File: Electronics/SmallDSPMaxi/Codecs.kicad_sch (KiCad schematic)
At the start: 56 parts, among them J13 IDC, J14 IDC, J15 IDC, J16 IDC

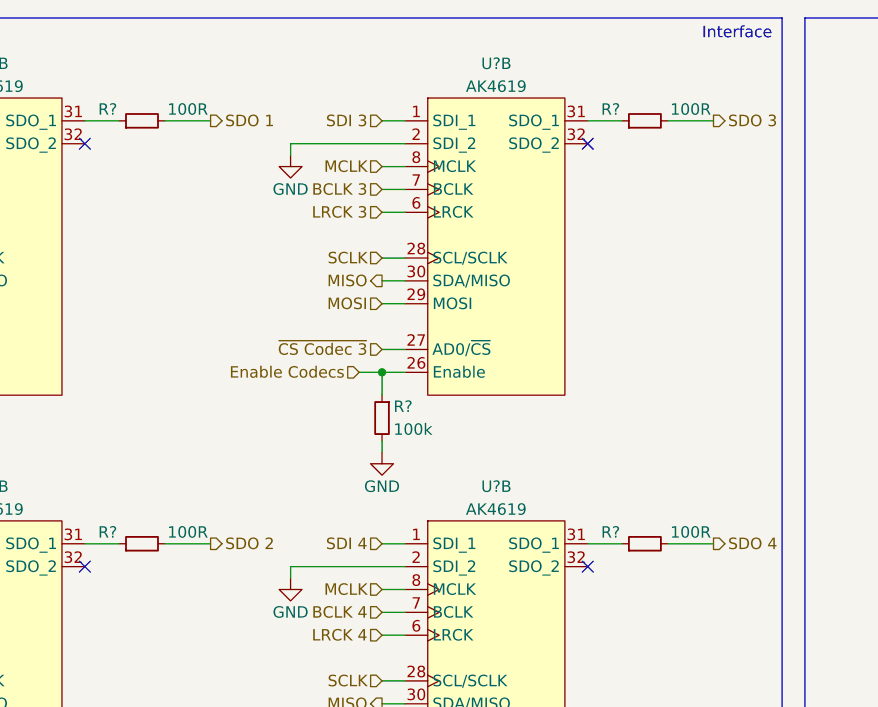
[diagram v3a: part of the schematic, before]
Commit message: Wires DSP programming port to SPI instead of I2C
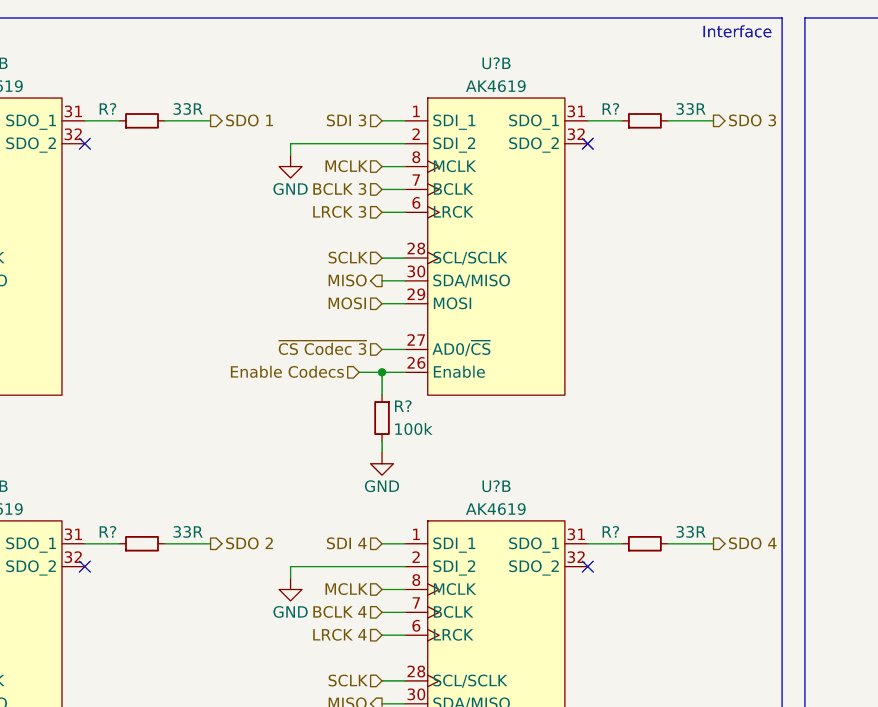
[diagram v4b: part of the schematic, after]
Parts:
- R? (x4): value 100R -> 33R; LCSC Part # C25076 -> C25105; Part Number 0402WGF1000TCE -> 0402WGF330JTCE
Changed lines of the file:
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@@
   (paper "A4")
   (title_block
-    (date "2023-10-24")
+    (date "2023-11-01")
   )
   (junction (at 250.19 114.3) (diameter 0) (color 0 0 0 0)
@@
       (effects (font (size 1.27 1.27)))
     )
-    (property "Value" "100R" (at 143.51 24.13 90)
+    (property "Value" "33R" (at 143.51 24.13 90)
       (effects (font (size 1.27 1.27)))
     )
@@
       (effects (font (size 1.27 1.27)) hide)
     )
-    (property "Part Number" "0402WGF1000TCE" (at 138.43 25.4 0)
+    (property "Part Number" "0402WGF330JTCE" (at 138.43 25.4 0)
       (effects (font (size 1.27 1.27)) hide)
     )
@@
       (effects (font (size 1.27 1.27)) hide)
     )
-    (property "LCSC Part #" "C25076" (at 138.43 25.4 0)
+    (property "LCSC Part #" "C25105" (at 138.43 25.4 0)
       (effects (font (size 1.27 1.27)) hide)
     )
@@
       (effects (font (size 1.27 1.27)))
     )
-    (property "Value" "100R" (at 199.39 24.13 90)
+    (property "Value" "33R" (at 199.39 24.13 90)
       (effects (font (size 1.27 1.27)))
     )
@@
       (effects (font (size 1.27 1.27)) hide)
     )
-    (property "Part Number" "0402WGF1000TCE" (at 194.31 25.4 0)
+    (property "Part Number" "0402WGF330JTCE" (at 194.31 25.4 0)
       (effects (font (size 1.27 1.27)) hide)
     )
@@
       (effects (font (size 1.27 1.27)) hide)
     )
-    (property "LCSC Part #" "C25076" (at 194.31 25.4 0)
+    (property "LCSC Part #" "C25105" (at 194.31 25.4 0)
       (effects (font (size 1.27 1.27)) hide)
     )
@@
       (effects (font (size 1.27 1.27)))
     )
-    (property "Value" "100R" (at 143.51 71.12 90)
+    (property "Value" "33R" (at 143.51 71.12 90)
       (effects (font (size 1.27 1.27)))
     )
@@
       (effects (font (size 1.27 1.27)) hide)
     )
-    (property "Part Number" "0402WGF1000TCE" (at 138.43 72.39 0)
+    (property "Part Number" "0402WGF330JTCE" (at 138.43 72.39 0)
       (effects (font (size 1.27 1.27)) hide)
     )
@@
       (effects (font (size 1.27 1.27)) hide)
     )
-    (property "LCSC Part #" "C25076" (at 138.43 72.39 0)
+    (property "LCSC Part #" "C25105" (at 138.43 72.39 0)
       (effects (font (size 1.27 1.27)) hide)
     )
@@
       (effects (font (size 1.27 1.27)))
     )
-    (property "Value" "100R" (at 199.39 71.12 90)
+    (property "Value" "33R" (at 199.39 71.12 90)
       (effects (font (size 1.27 1.27)))
     )
@@
       (effects (font (size 1.27 1.27)) hide)
     )
-    (property "Part Number" "0402WGF1000TCE" (at 194.31 72.39 0)
+    (property "Part Number" "0402WGF330JTCE" (at 194.31 72.39 0)
       (effects (font (size 1.27 1.27)) hide)
     )
@@
       (effects (font (size 1.27 1.27)) hide)
     )
-    (property "LCSC Part #" "C25076" (at 194.31 72.39 0)
+    (property "LCSC Part #" "C25105" (at 194.31 72.39 0)
       (effects (font (size 1.27 1.27)) hide)
     )

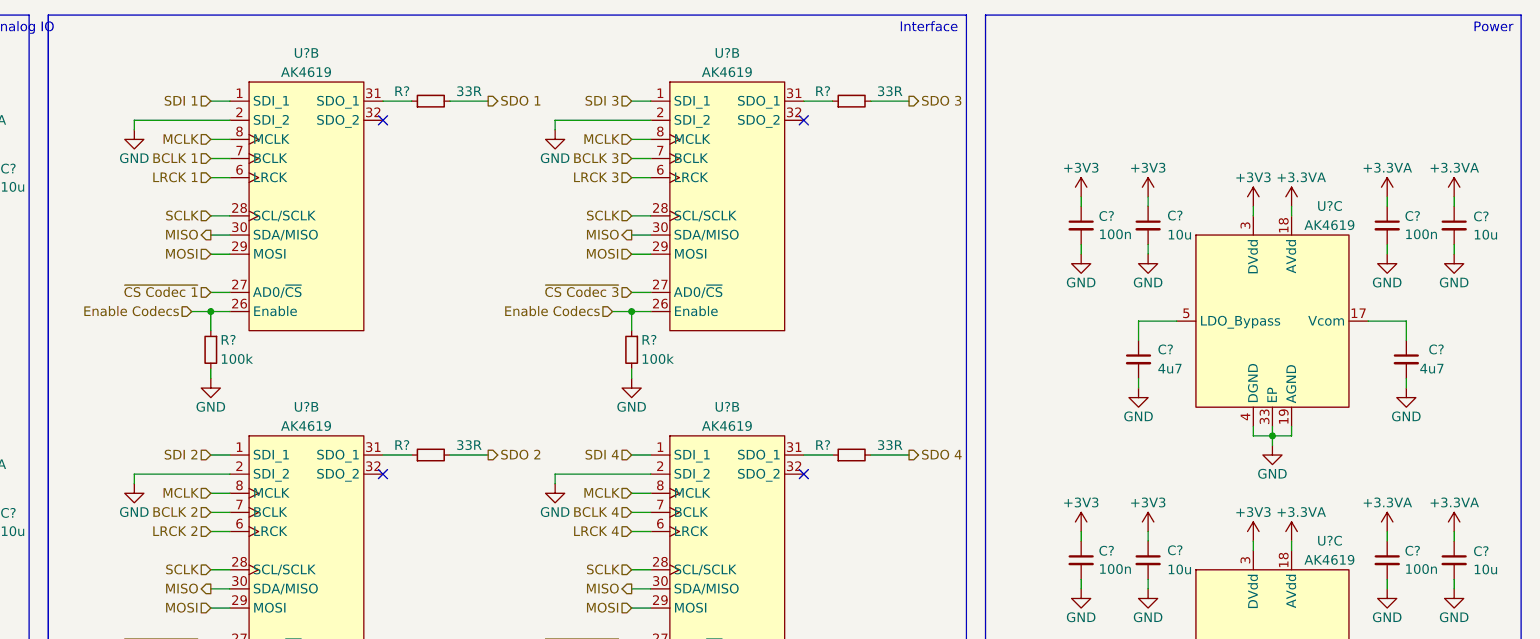
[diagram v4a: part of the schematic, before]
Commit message: Adds clock distributer
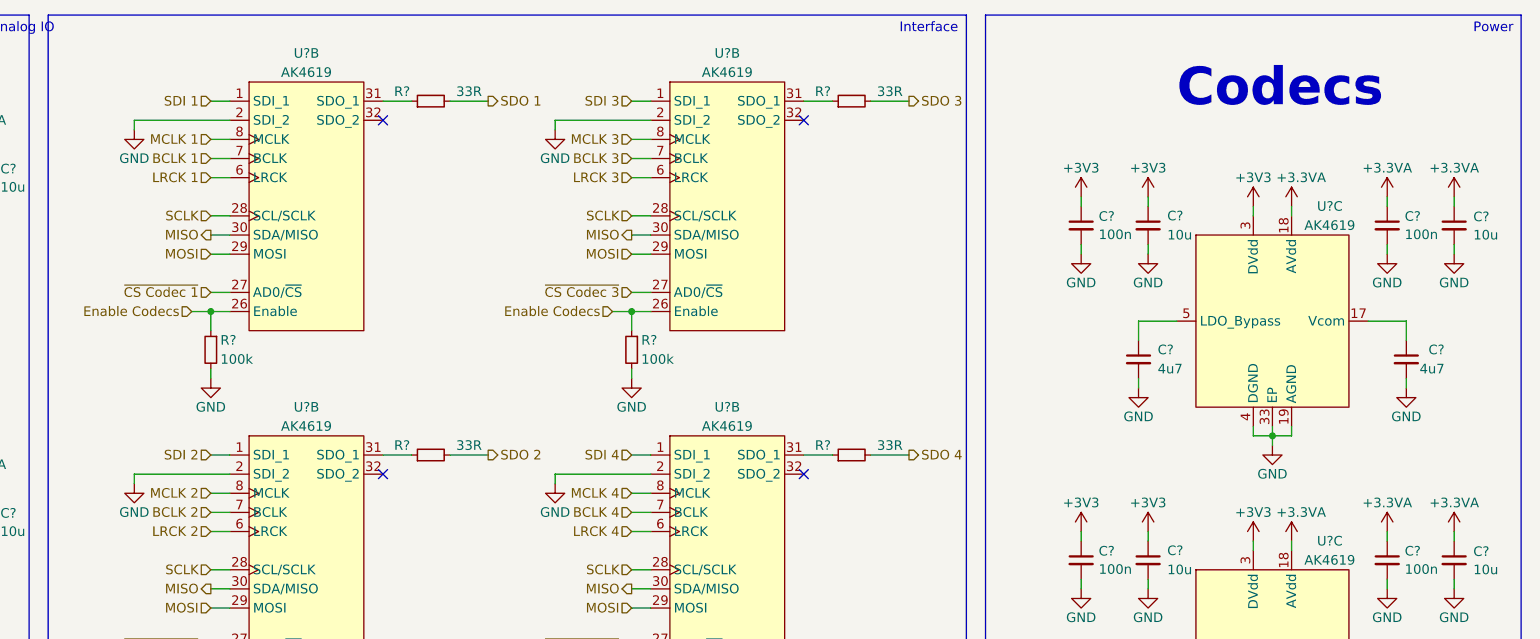
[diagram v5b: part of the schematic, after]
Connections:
- removed net MCLK: U?.8 (MCLK), U?.8 (MCLK), U?.8 (MCLK), U?.8 (MCLK)
- new net MCLK 1: U?.8 (MCLK)
- new net MCLK 2: U?.8 (MCLK)
- new net MCLK 3: U?.8 (MCLK)
- new net MCLK 4: U?.8 (MCLK)
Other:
- note added: "Codecs"
- company: (none) -> Till Heuer
- title: (none) -> SmallDSP Maxi

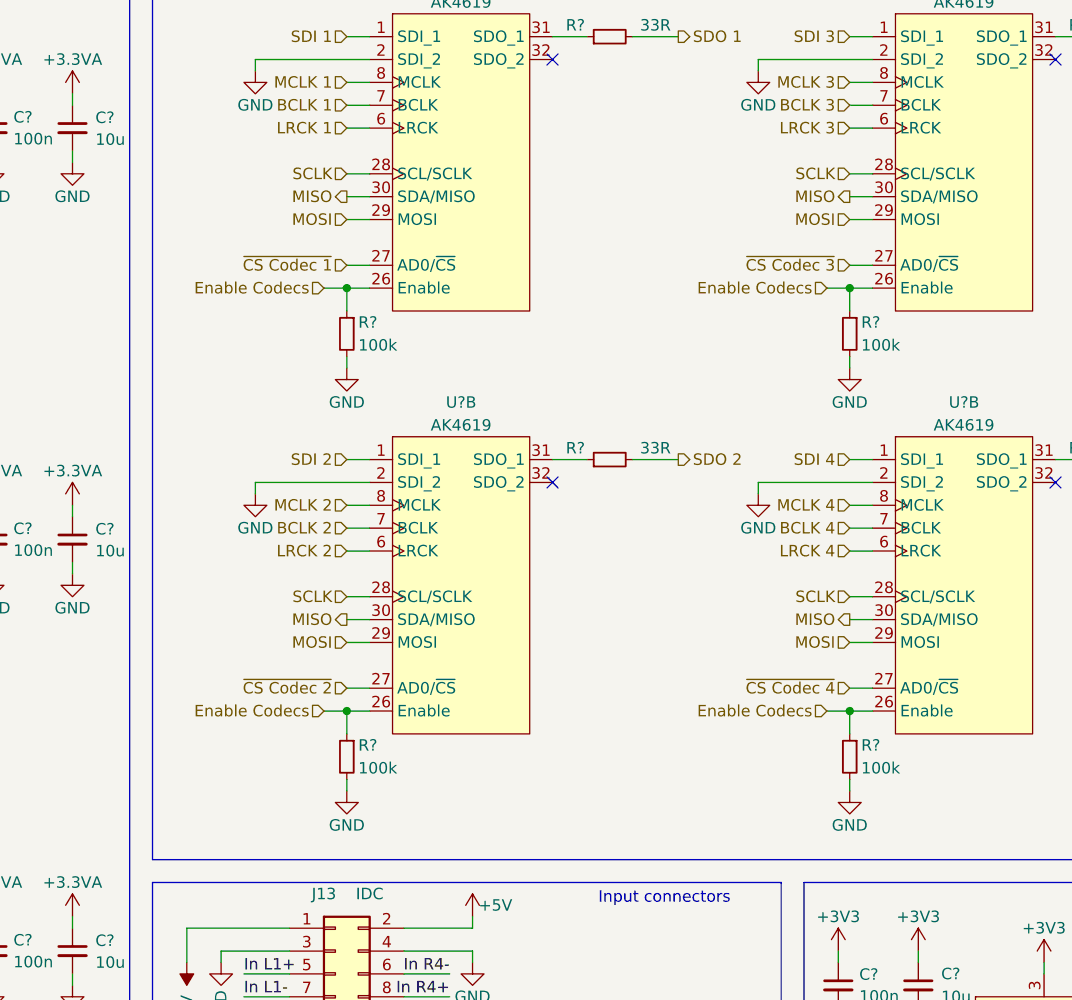
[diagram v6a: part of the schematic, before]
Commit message: adds usb to i2s bridge to micro. Adds tweaks for layout of maxi.
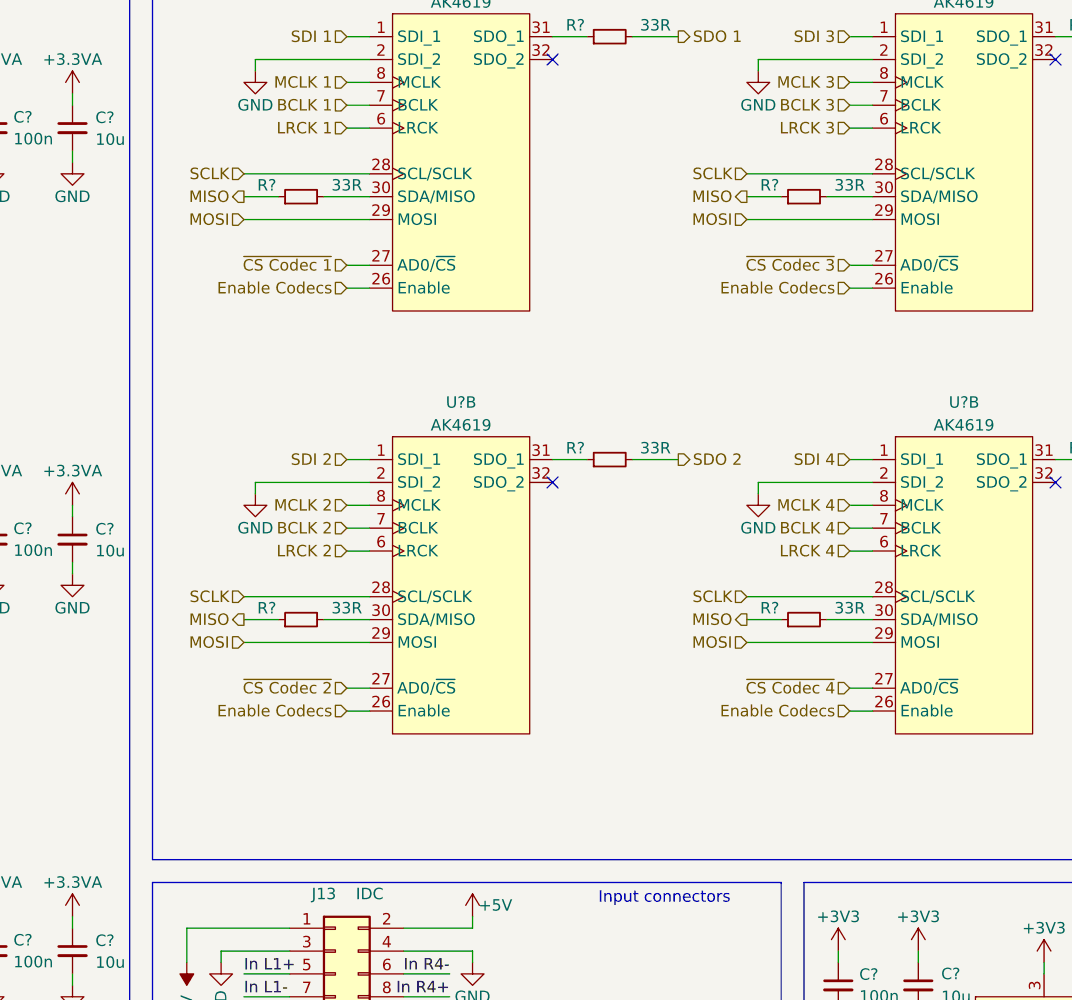
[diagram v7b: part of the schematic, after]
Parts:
- removed R? (x4): 100k, Resistor_SMD:R_0402_1005Metric, symbol Device:R_Small
- added R? (x4): 33R, Resistor_SMD:R_0402_1005Metric, symbol Device:R_Small
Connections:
- net MISO: now also R?.1, R?.1, R?.1, R?.1; no longer U?.30 (SDA/MISO), U?.30 (SDA/MISO), U?.30 (SDA/MISO), U?.30 (SDA/MISO)
- new net: R?.2, U?.30 (SDA/MISO) (x4)
